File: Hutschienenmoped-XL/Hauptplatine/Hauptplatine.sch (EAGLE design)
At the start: 138 parts, among them J1 638207222005, J13 638207222005, J15 638207222008, J2 645004114822, J4 61300421121, J7 638207222005, J8 638207222007, U4 TLE9250VSJ

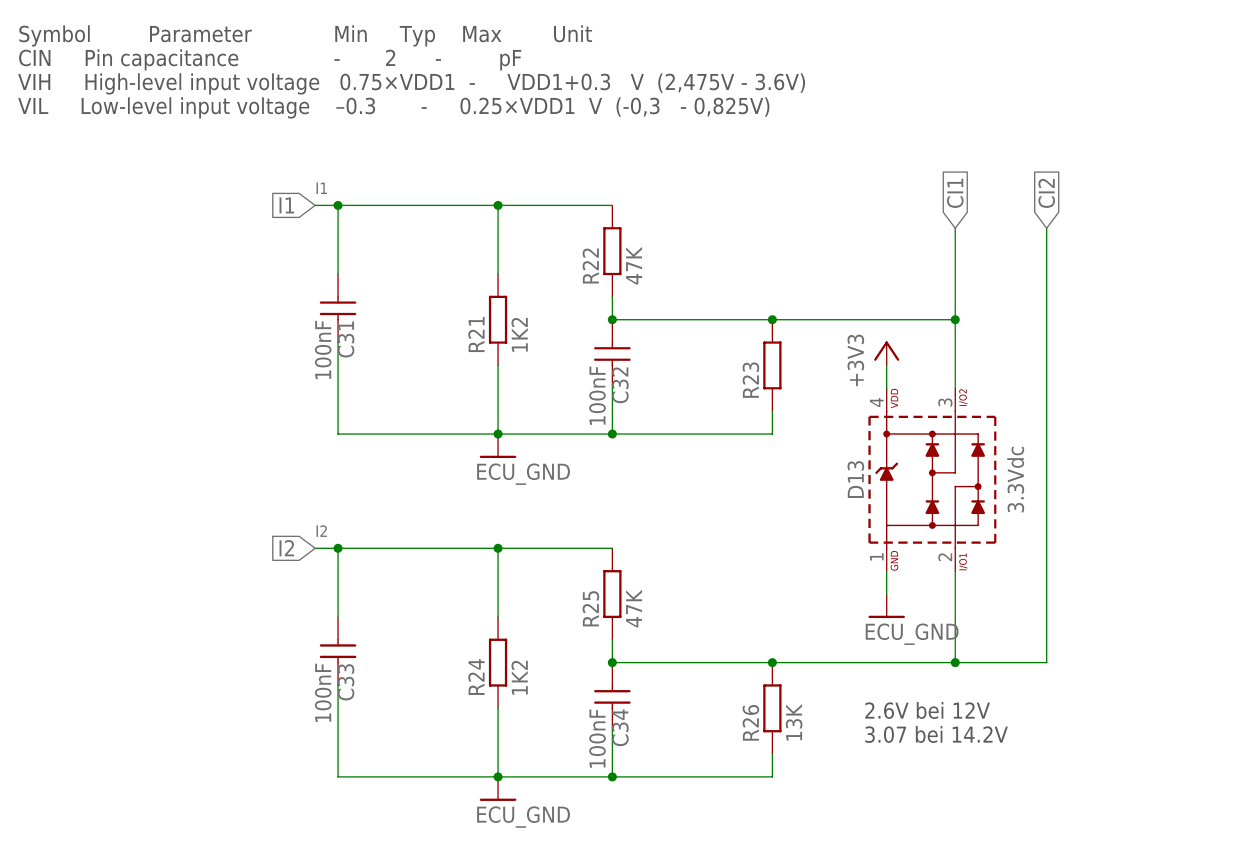
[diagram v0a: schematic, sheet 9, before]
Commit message: Updates resistor values and library URNs
Changes resistor values from 13k to 22k.

Updates library URNs in the eagle project file and board file.

Sets linktopcb3d to false in the board file.
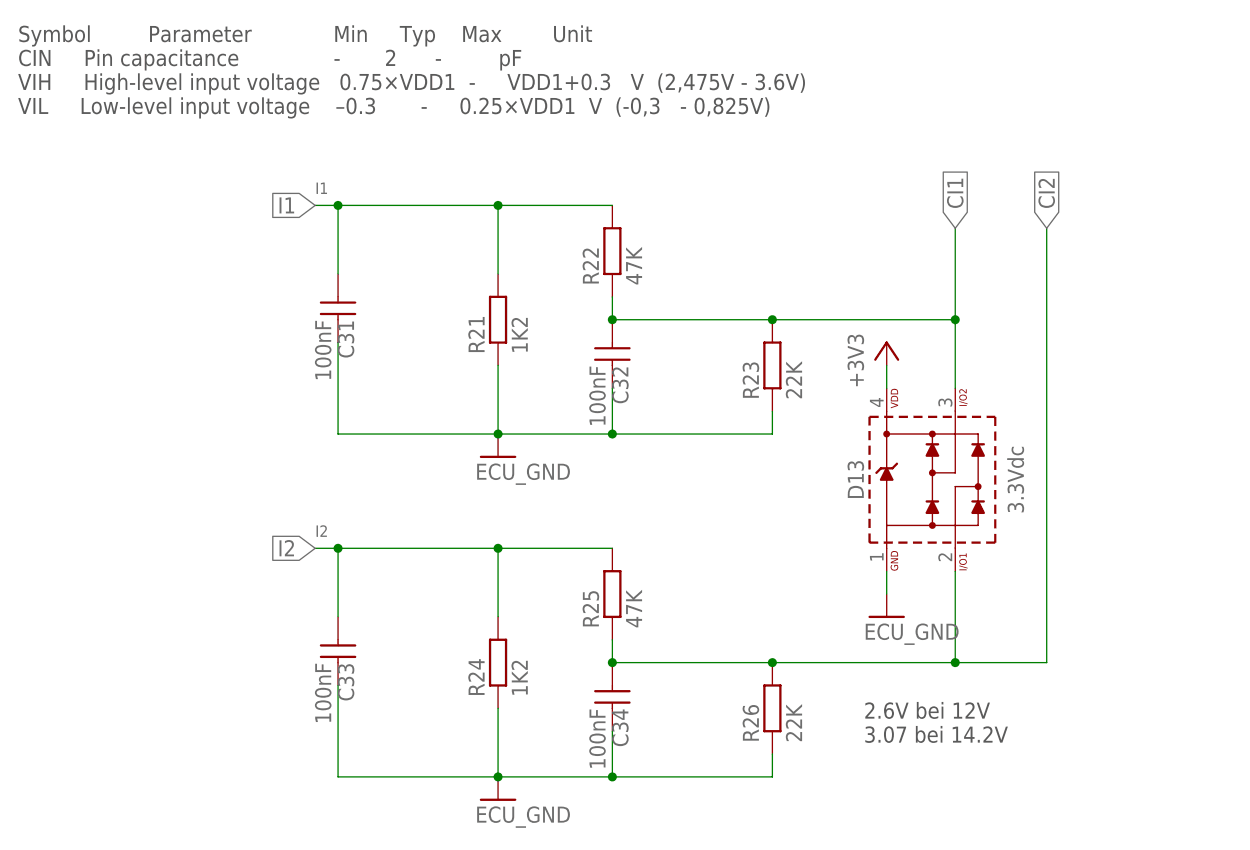
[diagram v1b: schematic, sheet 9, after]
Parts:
- R23, R26, R31, R32, R41, R44, R53, R56: value 13K -> 22K
